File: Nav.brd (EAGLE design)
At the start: 30 x 60 mm, 33 parts, among them SW5 THAU13-AB-R, SW6 THAU13-AB-R, SW7 TVAF06-A020B-R, SW8 TVAF06-A020B-R, U4 OPA340N, U5 DRIVER-LV8548MC-AH(SOIC10), U6 I-02247_NJM2845

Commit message: Add sensors
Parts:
- added U1: LSM9DS1, LSM9DS1:LGA24-8X4
- added U2: LPS25HB, LPS25HB:PQFN60P250X250X80-10N
- moved U$1 3.81 mm to (0.00, 14.0), turned to 90 degrees
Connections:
- new net GND-1: U2.8
- new net VDD_IO: U2.1
- net GND: now also U2.9
- net VDD: now also U2.10
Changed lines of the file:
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@@
 <attribute name="VALUE" x="-2.54" y="-5.4801" size="0.02" layer="27" rot="R270"/>
 </element>
-<element name="U$1" library="gps" package="GYSFFMANC" value="GYSFFMANC" x="0" y="17.78" smashed="yes"/>
+<element name="U$1" library="gps" package="GYSFFMANC" value="GYSFFMANC" x="0" y="13.97" smashed="yes" rot="R90"/>
+<element name="U1" library="LSM9DS1" package="LGA24-8X4" value="LSM9DS1" x="0" y="21.59" smashed="yes">
+<attribute name="NAME" x="-1.778" y="23.368" size="0.8128" layer="25"/>
+<attribute name="PROD_ID" value="IC-12536" x="0" y="21.59" size="1.778" layer="27" display="off"/>
+<attribute name="VALUE" x="-1.778" y="19.812" size="0.8128" layer="27" align="top-left"/>
+</element>
+<element name="U2" library="LPS25HB" package="PQFN60P250X250X80-10N" value="LPS25HB" x="6.35" y="21.59" smashed="yes">
+<attribute name="AVAILABILITY" value="In Stock" x="6.35" y="21.59" size="1.778" layer="27" display="off"/>
+<attribute name="DESCRIPTION" value=" Pressure Sensor 3.77PSI ~ 18.27PSI (26kPa ~ 126kPa) Absolute - 24 b 10-VFLGA " x="6.35" y="21.59" size="1.778" layer="27" display="off"/>
+<attribute name="MF" value="STMicroelectronics" x="6.35" y="21.59" size="1.778" layer="27" display="off"/>
+<attribute name="MP" value="LPS25HB" x="6.35" y="21.59" size="1.778" layer="27" display="off"/>
+<attribute name="NAME" x="3.84848125" y="23.29103125" size="1.27076875" layer="25"/>
+<attribute name="PACKAGE" value="VFLGA-10 STMicroelectronics" x="6.35" y="21.59" size="1.778" layer="27" display="off"/>
+<attribute name="PRICE" value="None" x="6.35" y="21.59" size="1.778" layer="27" display="off"/>
+<attribute name="PURCHASE-URL" value="https://pricing.snapeda.com/search/part/LPS25HB/?ref=eda" x="6.35" y="21.59" size="1.778" layer="27" display="off"/>
+<attribute name="VALUE" x="3.74815" y="18.788009375" size="1.2709" layer="27"/>
+</element>
 </elements>
 <signals>
@@
 <contactref element="U$1" pad="1"/>
 <contactref element="U$1" pad="44"/>
-<wire x1="-4.2" y1="14.98" x2="-4.3" y2="13.03" width="0" layer="19" extent="1-1"/>
-<wire x1="-4.2" y1="16.58" x2="-4.2" y2="14.98" width="0" layer="19" extent="1-1"/>
-<wire x1="-1.55" y1="16.23" x2="-4.2" y2="16.58" width="0" layer="19" extent="1-1"/>
-<wire x1="1.55" y1="16.23" x2="-1.55" y2="16.23" width="0" layer="19" extent="1-1"/>
-<wire x1="-1.55" y1="19.33" x2="-1.55" y2="16.23" width="0" layer="19" extent="1-1"/>
-<wire x1="-4.2" y1="20.58" x2="-1.55" y2="19.33" width="0" layer="19" extent="1-1"/>
-<wire x1="-4.3" y1="22.53" x2="-4.2" y2="20.58" width="0" layer="19" extent="1-1"/>
-<wire x1="-3.2" y1="22.38" x2="-4.3" y2="22.53" width="0" layer="19" extent="1-1"/>
-<wire x1="-2.4" y1="22.38" x2="-3.2" y2="22.38" width="0" layer="19" extent="1-1"/>
-<wire x1="-1.6" y1="22.38" x2="-2.4" y2="22.38" width="0" layer="19" extent="1-1"/>
-<wire x1="-0.8" y1="22.38" x2="-1.6" y2="22.38" width="0" layer="19" extent="1-1"/>
-<wire x1="0" y1="22.38" x2="-0.8" y2="22.38" width="0" layer="19" extent="1-1"/>
-<wire x1="0.8" y1="22.38" x2="0" y2="22.38" width="0" layer="19" extent="1-1"/>
-<wire x1="1.6" y1="22.38" x2="0.8" y2="22.38" width="0" layer="19" extent="1-1"/>
-<wire x1="4.3" y1="22.53" x2="1.6" y2="22.38" width="0" layer="19" extent="1-1"/>
-<wire x1="1.55" y1="19.33" x2="1.6" y2="22.38" width="0" layer="19" extent="1-1"/>
-<wire x1="4.3" y1="13.03" x2="1.55" y2="16.23" width="0" layer="19" extent="1-1"/>
-<wire x1="-13.55" y1="-12.785" x2="4.3" y2="22.53" width="0" layer="19" extent="1-16"/>
+<contactref element="U2" pad="9"/>
+<wire x1="8.5" y1="22.86" x2="4.75" y2="18.27" width="0" layer="19" extent="1-16"/>
+<wire x1="1.55" y1="12.42" x2="1" y2="15.36" width="0" layer="19" extent="1-16"/>
+<wire x1="1.2" y1="9.77" x2="0" y2="14.36" width="0" layer="19" extent="1-16"/>
+<wire x1="2.8" y1="9.77" x2="1.2" y2="9.77" width="0" layer="19" extent="1-1"/>
+<wire x1="-4.75" y1="18.27" x2="-6.35" y2="22.86" width="0" layer="19" extent="1-1"/>
+<wire x1="4.75" y1="9.67" x2="2.8" y2="9.77" width="0" layer="19" extent="1-1"/>
+<wire x1="-1.55" y1="12.42" x2="0" y2="14.36" width="0" layer="19" extent="1-16"/>
+<wire x1="-4.6" y1="15.57" x2="-4.75" y2="18.27" width="0" layer="19" extent="1-1"/>
+<wire x1="-4.6" y1="14.77" x2="-4.6" y2="15.57" width="0" layer="19" extent="1-1"/>
+<wire x1="-4.6" y1="13.97" x2="-4.6" y2="14.77" width="0" layer="19" extent="1-1"/>
+<wire x1="-4.6" y1="13.17" x2="-4.6" y2="13.97" width="0" layer="19" extent="1-1"/>
+<wire x1="-4.6" y1="12.37" x2="-4.6" y2="13.17" width="0" layer="19" extent="1-1"/>
+<wire x1="-4.6" y1="11.57" x2="-4.6" y2="12.37" width="0" layer="19" extent="1-1"/>
+<wire x1="-4.6" y1="10.77" x2="-4.6" y2="11.57" width="0" layer="19" extent="1-1"/>
+<wire x1="-4.75" y1="9.67" x2="-4.6" y2="10.77" width="0" layer="19" extent="1-1"/>
+<wire x1="-2.8" y1="9.77" x2="-4.75" y2="9.67" width="0" layer="19" extent="1-1"/>
+<wire x1="6.35" y1="22.51" x2="-4.75" y2="9.67" width="0" layer="19" extent="1-1"/>
+<wire x1="-1.55" y1="15.52" x2="-4.6" y2="15.57" width="0" layer="19" extent="1-1"/>
+<wire x1="1.55" y1="15.52" x2="1.55" y2="12.42" width="0" layer="19" extent="1-1"/>
 </signal>
 <signal name="VDD">
@@
 <wire x1="5.334" y1="2.54" x2="5.11" y2="2.764" width="0.508" layer="1"/>
 <wire x1="5.11" y1="2.764" x2="0.431" y2="2.764" width="0.508" layer="1"/>
+<contactref element="U2" pad="10"/>
+<wire x1="-10.16" y1="-10.16" x2="5.75" y2="22.51" width="0" layer="19" extent="1-1"/>
 </signal>
 <signal name="N$5">
@@
 <contactref element="U$1" pad="14"/>
 </signal>
+<signal name="VDD_IO">
+<contactref element="U2" pad="1"/>
+</signal>
+<signal name="GND-1">
+<contactref element="U2" pad="8"/>
+</signal>
 </signals>

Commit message: Navigation unit
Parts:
- added C1: (no value), rcl:C0603
- added C2: 10µF, rcl:C0603
- added C3, C4, C5: 0.1µF, rcl:C0603
- added C6: 0.01µF, rcl:C0603
- added J1: U.FL-R-SMT, connector:U.FL_SMT
- added R1, R2: 10k, rcl:R0603
- added SC: DCK-3R3E, capacitors:DC,DCK
- moved U2 12.7 mm to (-6.35, 21.6)
- moved U$1 3.81 mm to (3.81, 14.0), turned to 270 degrees
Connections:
- removed net GND-1: U2.8
- removed net VDD3V3: U$1.4
- removed net VDD3V3_BACKUP: U$1.14
- removed net VDD_IO: U2.1
- new net 1PPS: U$1.29
- new net ANT: J1.SIG, U$1.2
- new net GPS_!RESET!: U$1.32
- new net GPS_RTX: U$1.26
- new net GPS_TRX: U$1.25
- new net N$1: SC.+, U$1.14
- new net N$4: C6.1, U1.24
- new net N$6: C5.1, U1.21
- net GND: now also C1.2, C2.2, C3.2, C4.2, C5.2, C6.2, J1.GND1, J1.GND2, SC.-, U1.14, U1.15, U1.16, U1.17, U1.18, U1.19, U1.20, U2.3, U2.5, U2.8
- net I2C_SCL: now also R1.1, U1.2, U2.2
- net I2C_SDA: now also R2.1, U1.4, U2.4
- net VDD: now also C1.1, C2.1, C3.1, C4.1, R1.2, R2.2, U$1.4, U1.1, U1.22, U1.23, U1.3, U2.1, U2.6
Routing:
- net GND: track 222.8 -> 334.8 mm, vias 11 -> 14
- net VDD: track 131.7 -> 180.9 mm, vias 7 -> 10
- net I2C_SCL: track 0.00 -> 13.2 mm, vias 0 -> 2
- net I2C_SDA: track 0.00 -> 12.3 mm, vias 0 -> 1
- net N$1: track 0.00 -> 11.4 mm
- net N$6: track 0.00 -> 6.28 mm
- net N$4: track 0.00 -> 3.06 mm
- net ANT: track 0.00 -> 1.98 mm

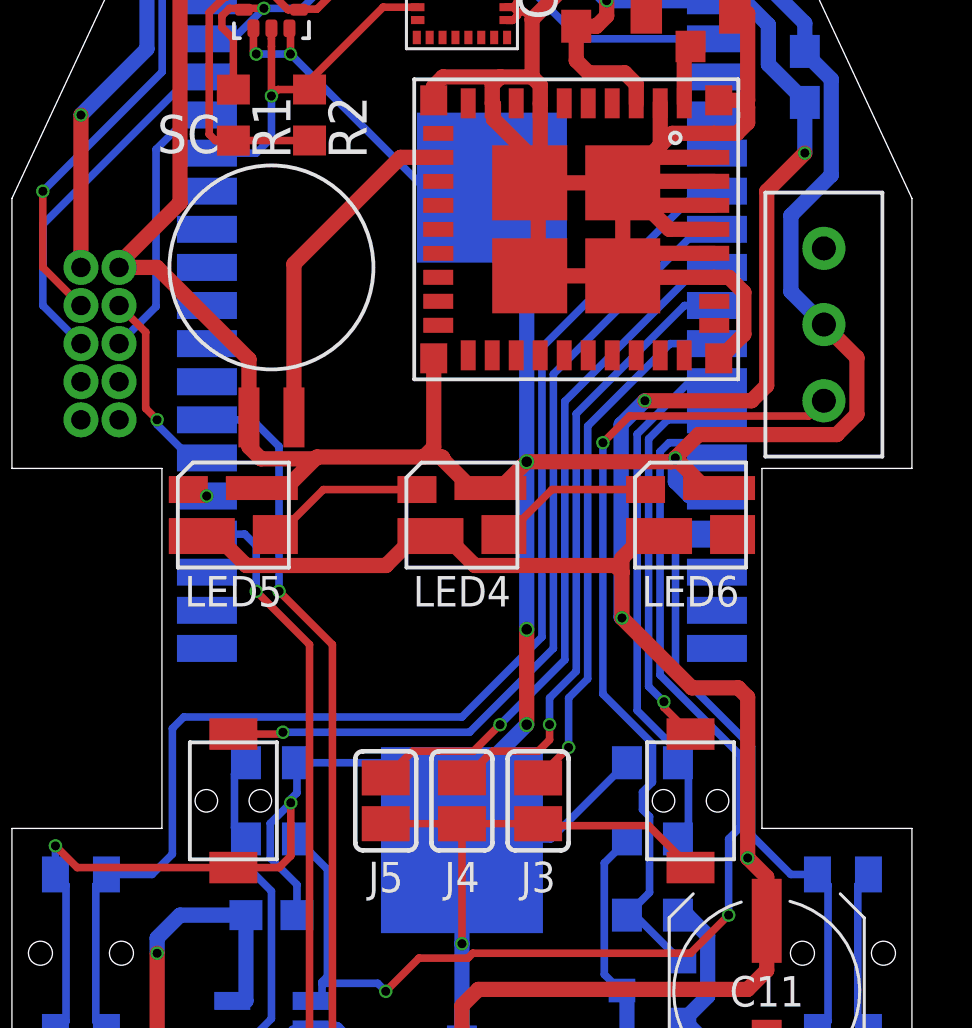
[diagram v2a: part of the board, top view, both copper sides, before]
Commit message: Fix analog input pins
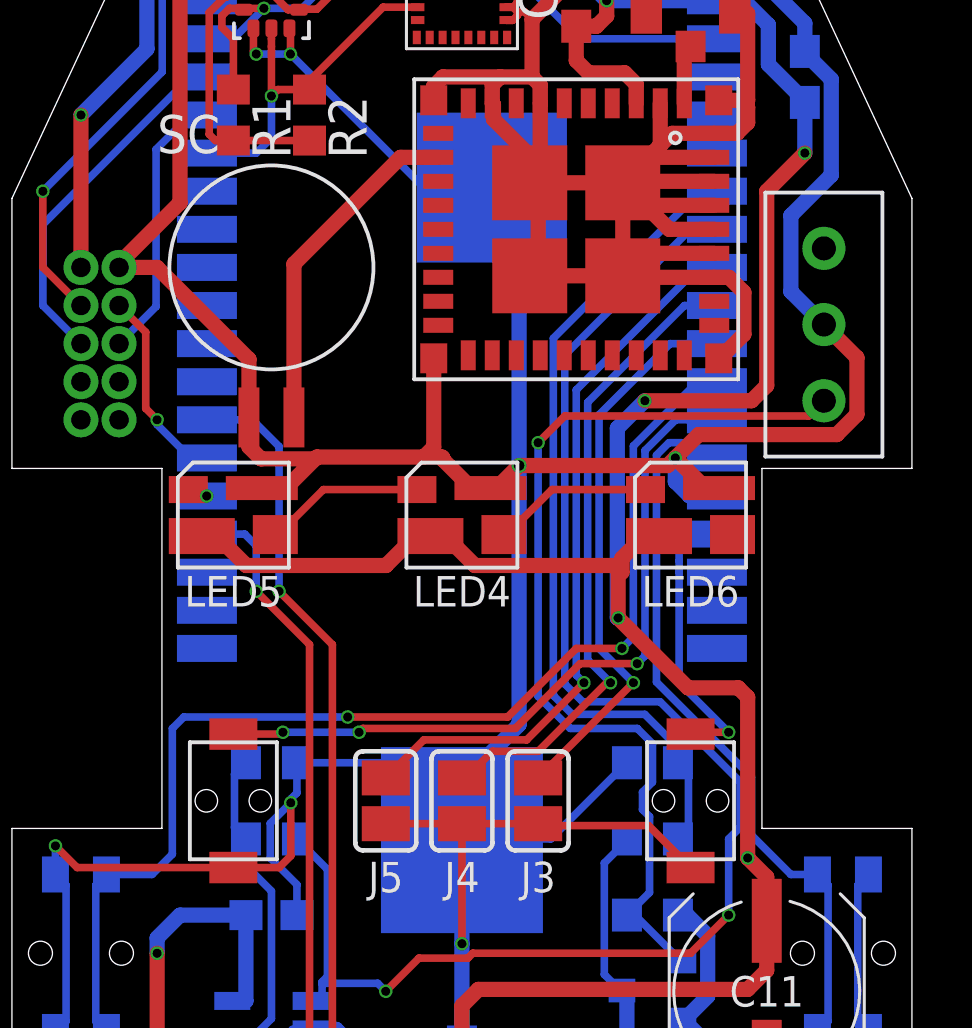
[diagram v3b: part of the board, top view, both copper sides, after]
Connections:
- net MSENSE: now also U$2.IO32; no longer U$2.IO12
- net SW1: now also U$2.IO12; no longer U$2.IO13
- net SW2: now also U$2.IO27; no longer U$2.IO35
- net SW3: now also U$2.IO13; no longer U$2.IO14
- net SW4: now also U$2.IO14; no longer U$2.IO32
- net VSENSE: now also U$2.IO35; no longer U$2.IO27
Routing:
- net MSENSE: track 39.9 -> 50.6 mm
- net VSENSE: track 17.7 -> 27.6 mm
- net SW2: track 43.4 -> 38.9 mm, vias 0 -> 2
- net N$10: track 27.4 -> 31.8 mm
- net SW1: track 20.5 -> 24.7 mm
- net SW4: track 28.4 -> 24.5 mm, vias 1 -> 3
- net SW3: track 13.0 -> 9.62 mm
- net J2: track 23.1 -> 24.2 mm
- net J0: track 17.9 -> 18.8 mm
- net J1: track 20.9 -> 21.6 mm
- net GND: track 334.8 -> 334.5 mm, vias 14 -> 12

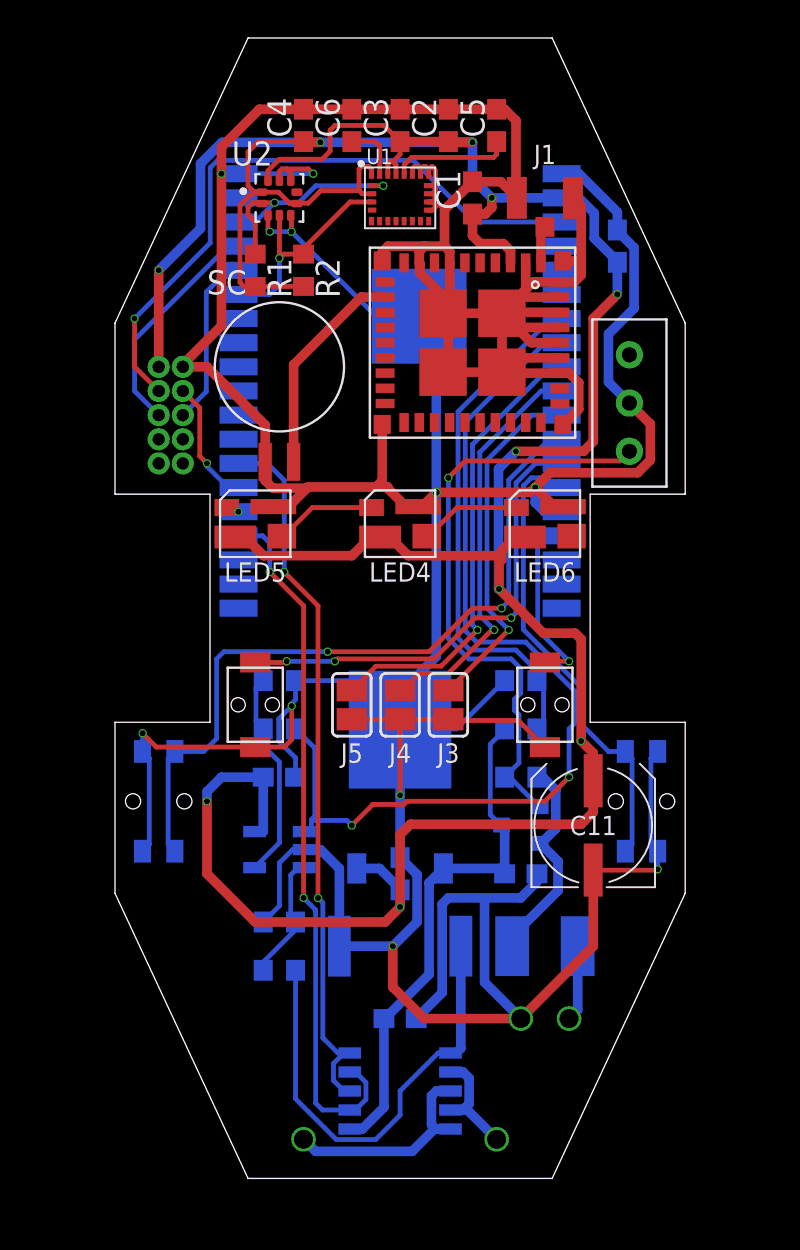
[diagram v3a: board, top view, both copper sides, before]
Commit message: reduce switch pins
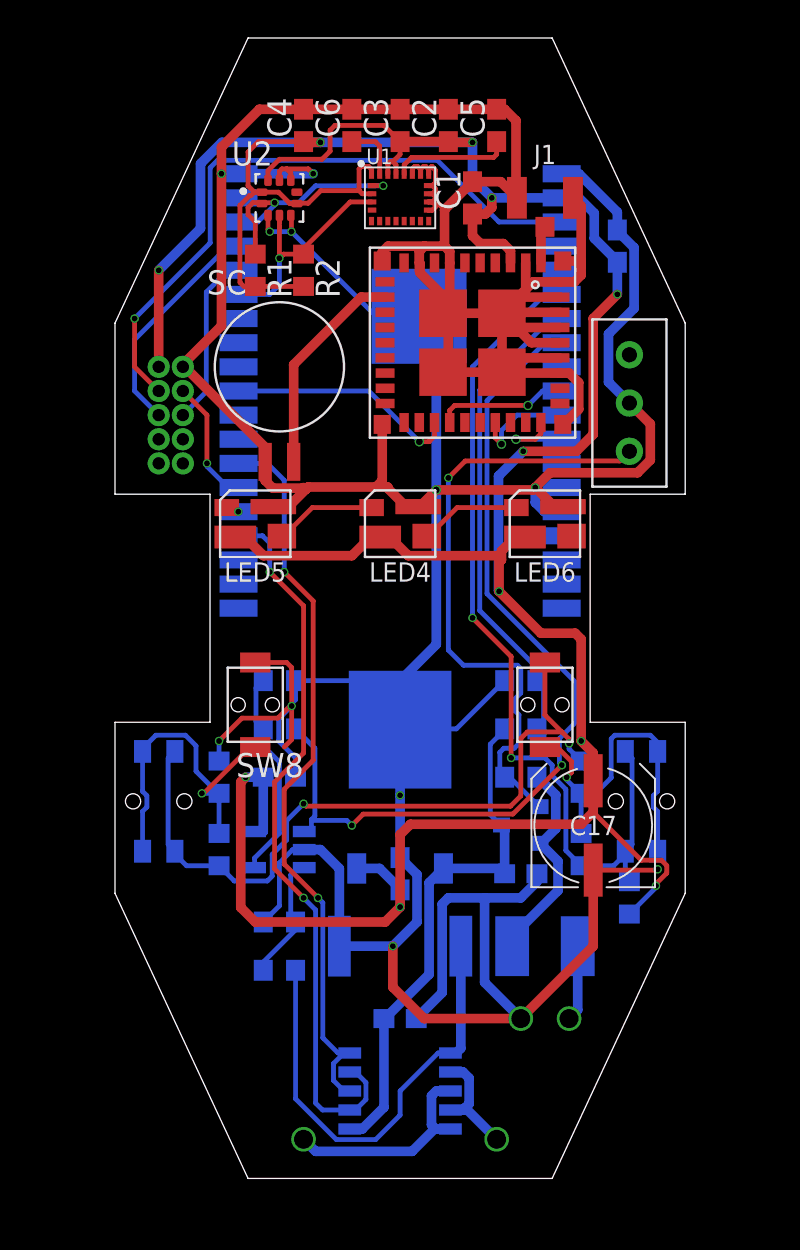
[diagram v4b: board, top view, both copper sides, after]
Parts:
- removed J3, J4, J5: (no value), jumper:SJ
- removed U$2: ESP32-WROVER-E, esp32:ESP32-WROVER-E
- removed U4: OPA340N, burr-brown:SOT23-5
- added R22, R23, R24, R25, R26: (no value), rcl:R0603
- added U$7: P2_5_1.27, pins:P2_5_1.27
- added U8: I-02247_NJM2845, akizuki:TO252
- U$4: value SS12D01GX -> ESP32-WROVER-E; device switches:SS12D01GX -> esp32:ESP32-WROVER-E
- U$5: value P2_5_1.27 -> SS12D01GX; device pins:P2_5_1.27 -> switches:SS12D01GX
- U6: value I-02247_NJM2845 -> OPA340N; device akizuki:TO252 -> burr-brown:SOT23-5
- moved U$5 24.8 mm to (12.1, 10.8), turned to 90 degrees
- moved U$4 12.1 mm to (0.00, 11.4), flipped to the bottom, turned to 0 degrees
- moved U6 7.41 mm to (-6.35, -12.7), turned to 270 degrees
- turned SW7 to 180 degrees
- turned SW8 to 180 degrees
- renumbered C10 to C16, C11 to C17, C12 to C18, C7 to C13, C8 to C14, C9 to C15, R10 to R17, R11 to R18, R12 to R19, R13 to R20, R14 to R21, R8 to R15, R9 to R16, U5 to U7
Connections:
- removed net J0: J3.1, U$2.IO26
- removed net J1: J4.1, U$2.IO25
- removed net J2: J5.1, U$2.IO33
- removed net N$10: R21.1, T1.3, U$4.1
- removed net N$8: R15.2, R16.1, U4.4
- removed net N$9: R17.2, R18.1, U4.3
- removed net SPI_CLK: U$2.IO18
- removed net SPI_CS: U$2.IO5
- removed net SPI_MISO: U$2.IO19
- removed net SW1: SW6.1, SW6.2, U$2.IO12
- removed net SW2: SW5.1, SW5.2, U$2.IO27
- removed net SW3: SW7.P$1, U$2.IO13
- removed net SW4: SW8.P$1, U$2.IO14
- new net N$14: R15.2, R16.1, U6.4
- new net N$15: R17.2, R18.1, U6.3
- new net N$16: R21.1, T1.3, U$5.1
- new net N$19: R24.1, R25.2, SW5.1, SW5.2, SW7.P$2
- new net N$20: R23.1, R24.2, SW6.3, SW6.4, SW7.P$1
- new net N$21: R25.1, R26.2, SW5.3, SW5.4, SW8.P$1
- new net SW: R22.1, R23.2, SW6.1, SW6.2, U$4.IO34
- net 1: now also U$7.P7; no longer U$5.P7
- net 1PPS: now also U$4.IO26
- net 2: now also U$7.P8; no longer U$5.P8
- net 3: now also U$7.P9; no longer U$5.P9
- net 4: now also U$7.P10; no longer U$5.P10
- net GND: now also R26.1, U$4.GND1, U$4.GND2, U$4.GND3, U$4.P_GND, U$5.2, U$7.P2, U8.2; no longer J3.2, J4.2, J5.2, SW5.3, SW5.4, SW6.3, SW6.4, SW7.P$2, U$2.GND1, U$2.GND2, U$2.GND3, U$2.P_GND, U$4.2, U$5.P2, U4.2
- net GPS_!RESET!: now also U$4.IO27
- net GPS_RTX: now also U$4.IO25
- net GPS_TRX: now also U$4.IO5
- net I2C_SCL: now also U$4.IO22; no longer U$2.IO22
- net I2C_SDA: now also U$4.IO21; no longer U$2.IO21
- net LED: now also U$4.IO2; no longer U$2.IO2
- net MC1: now also U$4.IO15; no longer U$2.IO15
- net MC2: now also U$4.IO4; no longer U$2.IO4
- net MSENSE: now also U$4.IO32, U6.1; no longer U$2.IO32, U4.1
- net PRG: now also U$4.IO0, U$7.P4; no longer U$2.IO0, U$5.P4
- net RESET: now also U$4.EN, U$7.P3; no longer U$2.EN, U$5.P3
- net RX: now also U$4.RXD0, U$7.P6; no longer U$2.RXD0, U$5.P6
- net TX: now also U$4.TXD0, U$7.P5; no longer U$2.TXD0, U$5.P5
- net VCC: now also U8.1; no longer U6.1
- net VDD: now also R22.2, U$4.3V3, U$7.P1, U6.5, U8.3; no longer U$2.3V3, U$5.P1, U4.5, U6.3
- net VSENSE: now also U$4.IO35; no longer U$2.IO35
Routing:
- net SW: track 0.00 -> 45.9 mm, vias 0 -> 2
- net N$19: track 0.00 -> 39.0 mm, vias 0 -> 2
- net SW2: track 38.9 -> 0.00 mm, vias 2 -> 0
- net N$16: track 0.00 -> 32.7 mm, vias 0 -> 1
- net N$10: track 31.8 -> 0.00 mm, vias 1 -> 0
- net GND: track 334.5 -> 308.3 mm
- net SW1: track 24.7 -> 0.00 mm
- net SW4: track 24.5 -> 0.00 mm, vias 3 -> 0
- net J2: track 24.2 -> 0.00 mm, vias 1 -> 0
- net J1: track 21.6 -> 0.00 mm, vias 1 -> 0
- net J0: track 18.8 -> 0.00 mm, vias 1 -> 0
- net N$21: track 0.00 -> 18.8 mm, vias 0 -> 1
- net N$20: track 0.00 -> 18.5 mm, vias 0 -> 1
- net GPS_TRX: track 0.00 -> 12.3 mm, vias 0 -> 1
- net N$8: track 11.6 -> 0.00 mm
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
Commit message: change parts name
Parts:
- removed C13, C18: 0.1µF, rcl:C0603
- removed C14: 1µF, rcl:C0603
- removed C15: 0.33µF, rcl:C0603
- removed C16: 2.2µF, rcl:C0603
- removed C17: 220µF, rcl:UD-6,3X7,7_NICHICON
- removed R19: 200k, rcl:R0603
- removed R21: 100k, rcl:R0603
- added C10, C11, C9: 0.1µF, rcl:C0603
- added C12: 10µF, rcl:C0603
- added C7: (no value), rcl:C0603
- added C8: 0.01µF, rcl:C0603
- added R14: 10k, rcl:R0603
- added R6: 1k, rcl:R0603
- C1: value (none) -> 0.33µF
- C2: value 10µF -> 2.2µF
- C3: value 0.1µF -> 220µF; device rcl:C0603 -> rcl:UD-6,3X7,7_NICHICON
- C5: value 0.1µF -> 1µF
- C6: value 0.01µF -> 0.1µF
- R1: value 10k -> 100k
- R15: value 1k -> 10k
- R2: value 10k -> 200k
- moved C5 47.3 mm to (0.00, -21.6), flipped to the bottom, turned to 0 degrees
- moved C2 39.5 mm to (0.00, -14.0), flipped to the bottom
- moved C3 38.2 mm to (10.2, -11.4)
- moved C1 35.7 mm to (6.35, -14.0), flipped to the bottom, turned to 180 degrees
- moved C6 34.5 mm to (-6.35, -8.89), flipped to the bottom, turned to 180 degrees
- moved R1 30.1 mm to (6.35, -8.89), flipped to the bottom, turned to 180 degrees
- moved R2 26.7 mm to (6.35, -6.35), flipped to the bottom, turned to 0 degrees
- moved R15 21.6 mm to (-5.08, 17.8), flipped to the top, turned to 270 degrees
- moved C4 17.7 mm to (11.4, 19.1), flipped to the bottom
- renumbered R16 to R8, R17 to R4, R18 to R7, R20 to R3, R22 to R9, R23 to R10, R24 to R11, R25 to R12, R26 to R13, RS1 to R5
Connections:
- net GND: now also C10.2, C11.2, C12.2, C3.-, C5.1, C7.2, C8.2, C9.2, R6.1; no longer C13.2, C14.1, C15.2, C16.2, C17.-, C18.2, C3.2, C5.2, R15.1
- net I2C_SCL: now also R14.1; no longer R1.1
- net I2C_SDA: now also R15.1; no longer R2.1
- net N$13: now also R1.2; no longer R21.2
- net N$14: now also R6.2; no longer R15.2
- net N$16: now also R1.1; no longer R21.1
- net N$4: now also C8.1; no longer C6.1
- net N$6: now also C9.1; no longer C5.1
- net VCC: now also C1.1, C5.2, R2.2; no longer C14.2, C15.1, R19.2
- net VDD: now also C10.1, C11.1, C12.1, C3.+, C6.1, C7.1, R14.2, R15.2; no longer C1.1, C13.1, C16.1, C17.+, C18.1, C3.1, R1.2, R2.2
- net VSENSE: now also R2.1; no longer R19.1

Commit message: Format silk
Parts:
- renumbered LED4 to LED2, LED5 to LED3, LED6 to LED1, SW5 to SW2, SW6 to SW1, SW7 to SW3, SW8 to SW4
